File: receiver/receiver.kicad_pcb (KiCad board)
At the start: 4 copper layers, 20.2 x 28 mm, 22 parts, among them J1 CONN_04SCREW, U1 10118194-MICRO-USB, U2 LM3671MF-3.3/NOPBMF05A-M, U3 SN74LVC2T45DCTRE4, U5 FT231XQ-R, U6 MBT3904DW1T1G

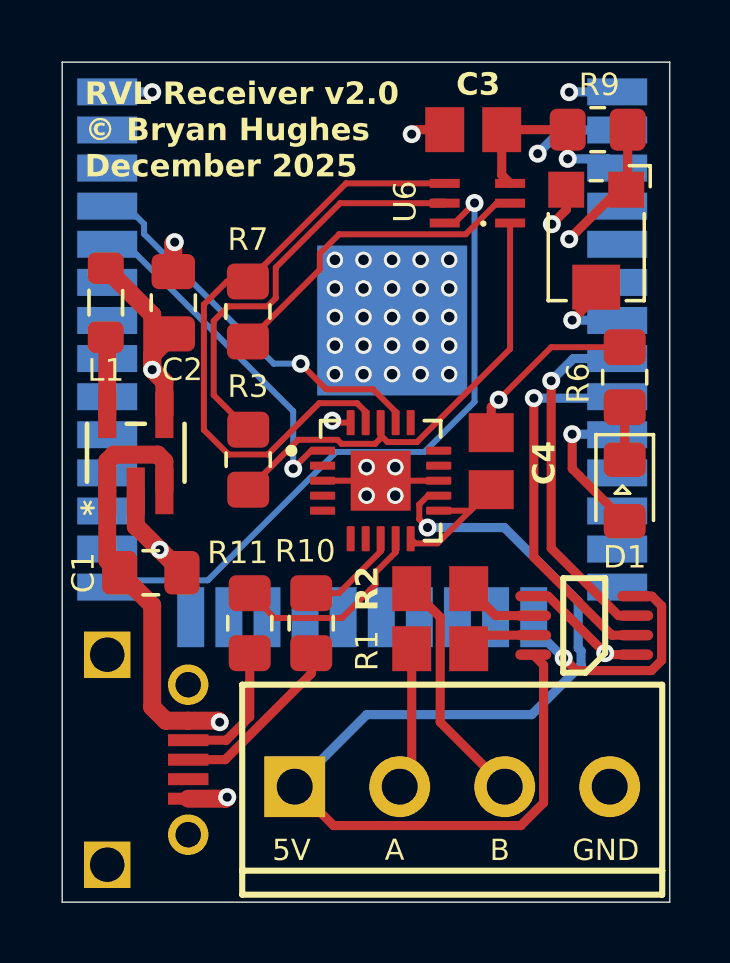
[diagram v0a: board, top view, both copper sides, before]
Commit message: Started redesigning receiver
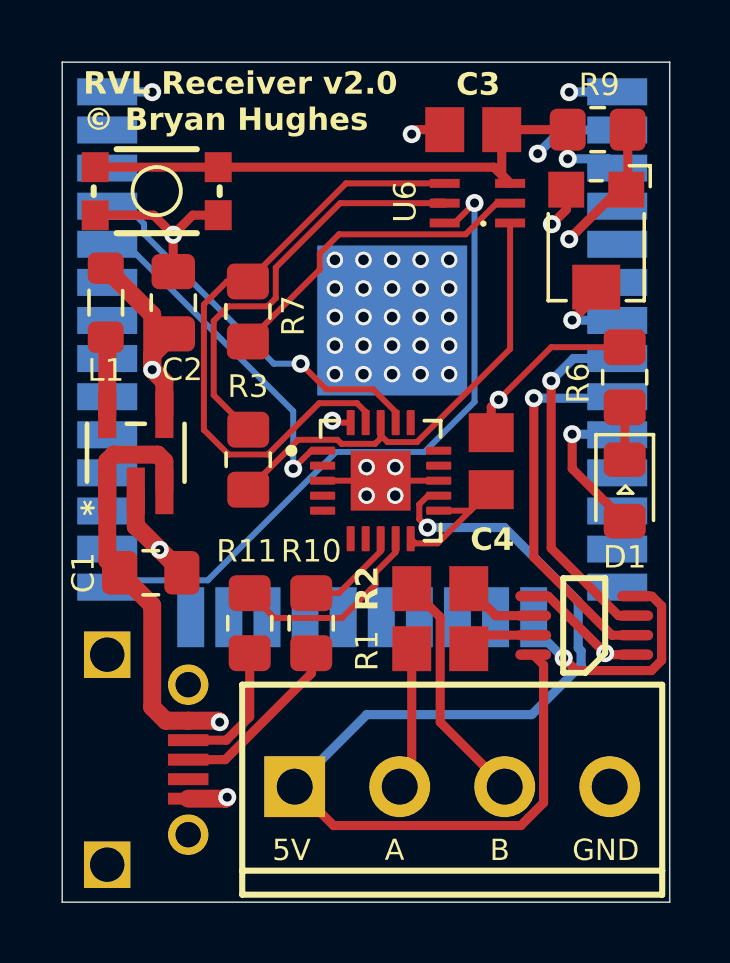
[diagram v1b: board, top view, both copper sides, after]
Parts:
- added S1: ~, receiver:TACTILE_SWITCH_SMD_4.6X2.8MM, F.Cu at (106.2, 118.3)
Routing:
- net EN: track 6.86 -> 20.9 mm
- net GND: track 30.2 -> 35.1 mm
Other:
- board text added: "RVL Receiver v2.0 © Bryan Hughes"
- board text removed: "RVL Receiver v2.0 © Bryan Hughes December 2025"
